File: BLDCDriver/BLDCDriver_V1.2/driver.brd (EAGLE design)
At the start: 42 x 50 mm, 75 parts, among them Q2 SIZ240DT-T1-GE3, Q3 SIZ240DT-T1-GE3, Q4 SIZ240DT-T1-GE3, U1 QFN50P400X400X100-25NDRV8300D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, U2 AS5048A-HTSP-500, U3 MCP2562-E/SN, U4 SOP80P620X125-8N, X1 JST-XH-07-PIN-ROUND-PAD, X2 JST-XH-06-PIN-LONG-PAD

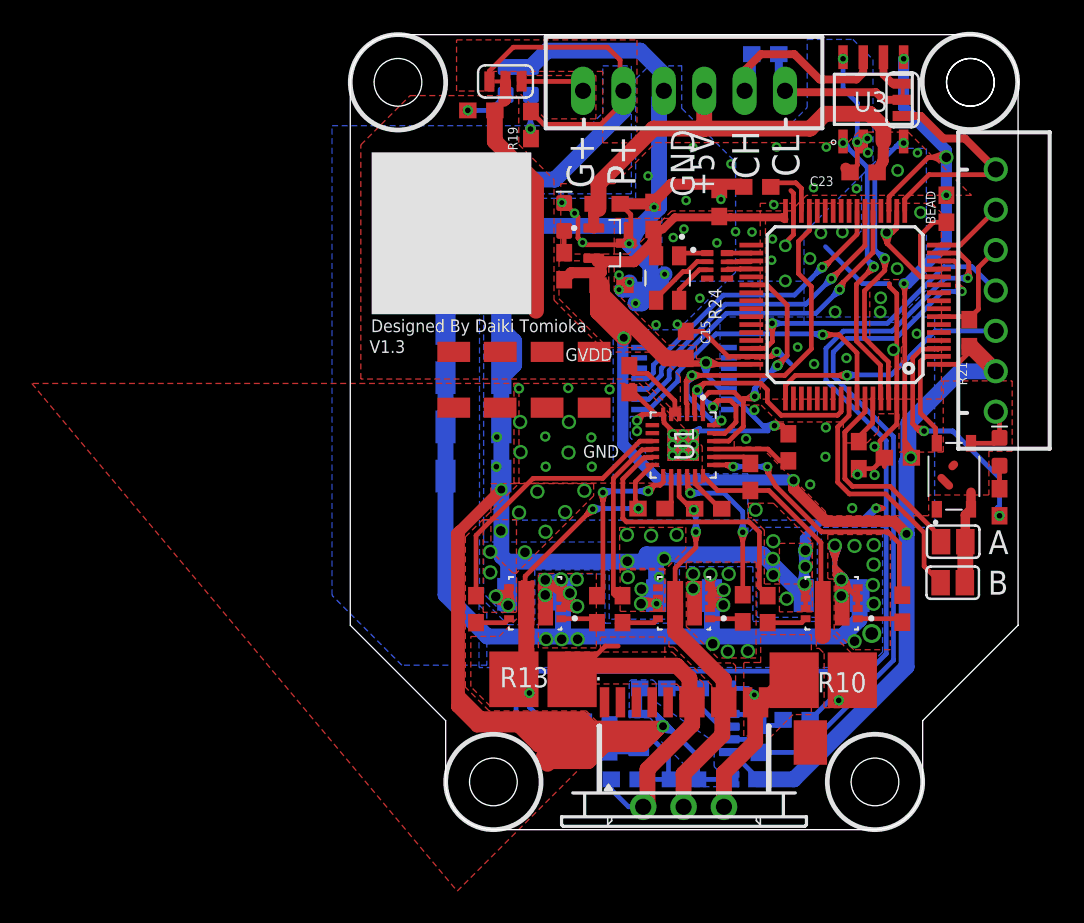
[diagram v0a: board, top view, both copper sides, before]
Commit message: :sparkles: V1.4 JLCPCBのPCBA検証用基板の設計DONE
# ==== Emojis ====
# ✨ :sparkles: Add new feature
# ✅  :white_check_mark: Update existing feature (not bug)
# ⚠️  :warning: Fix bug/error
# 🔥  :fire: Remove files or features
# ✏️ :pencil2: Fix typos
# 📝  :memo: Update documentation
# ♻️  :recycle: Dependencies update
# 🐧  :penguin: Improved the Linux
# 🍎  :apple: Improved the macOS
# 🔖 :bookmark: Add new library
# 🎉  :tada: Initial commit

# ==== Format ====
# :emoji: Subject
#
# Commit body...

# ==== Messages ====
# 新規(ファイル)機能追加: Add
# 機能修正、既存機能追加（バグではない): Update
# リファクタリング: Clean
# ファイル名変更:
# 削除など: Remove
# バグ修正: Fix
# バージョンアップ: Upgrade
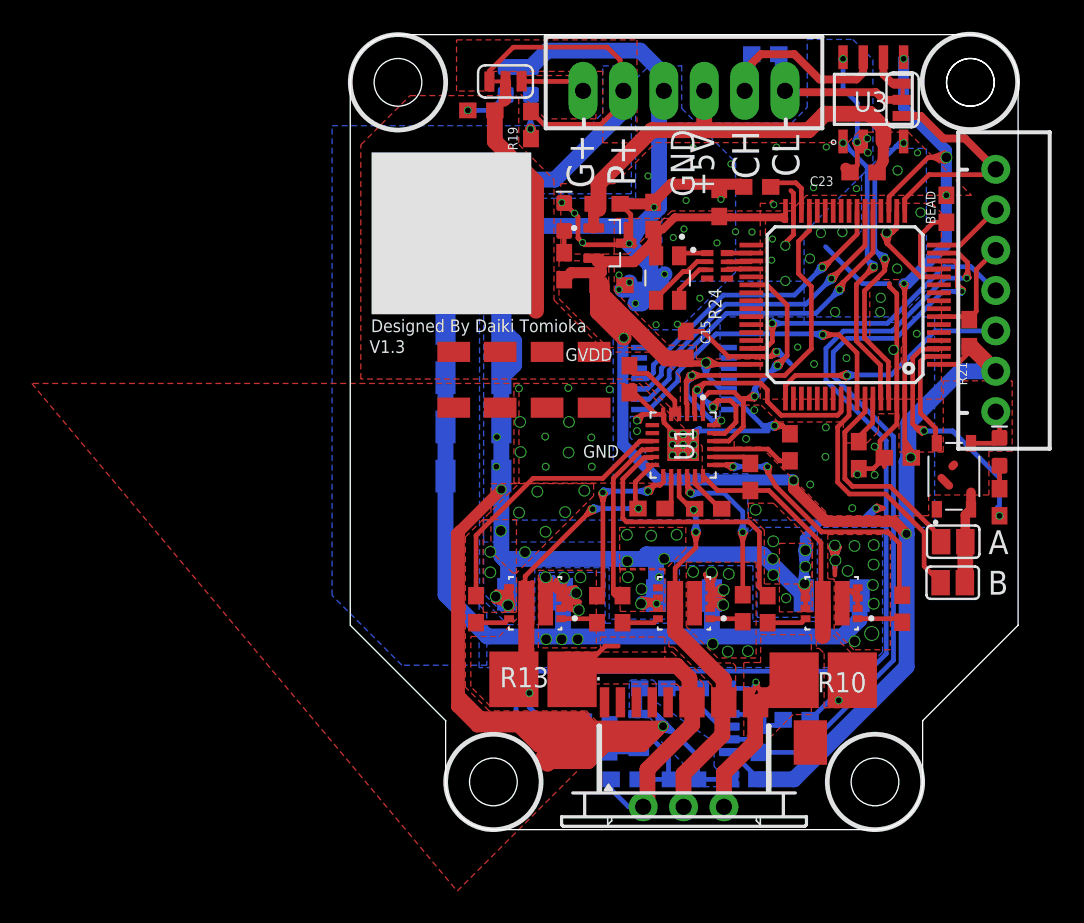
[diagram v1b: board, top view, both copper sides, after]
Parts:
- moved R7 0.10 mm to (28.2, 25.0)
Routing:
- net PVDD: track 158.3 -> 146.9 mm, vias 28 -> 26
- net C_W: track 71.6 -> 70.3 mm
- net W_CS: track 15.7 -> 16.3 mm
